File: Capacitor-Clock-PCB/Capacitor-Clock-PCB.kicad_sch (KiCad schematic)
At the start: 14 parts, among them J1 Jack-DC, J2 Conn_01x04, J3 Conn_01x02, J4 Conn_01x05, J5 Conn_01x02, J6 Conn_01x05, U2 DS3231M

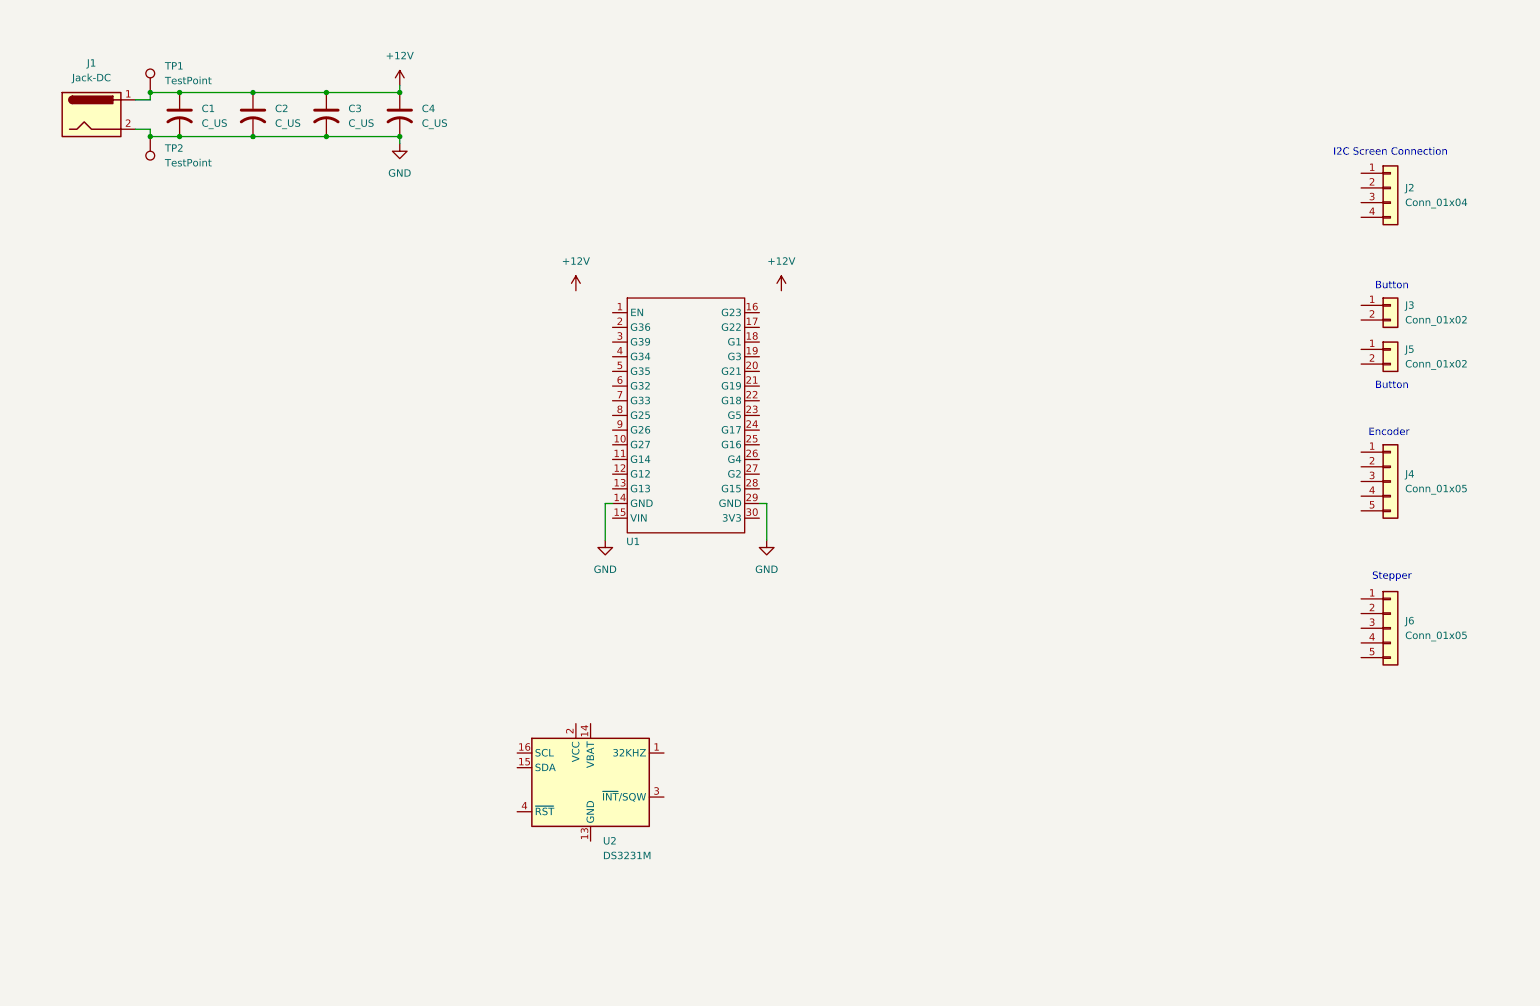
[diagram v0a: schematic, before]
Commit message: Preliminary Schematic Finished
Finished the schematic for the clock and is ready for review. going to continue to pcb layout in meantime
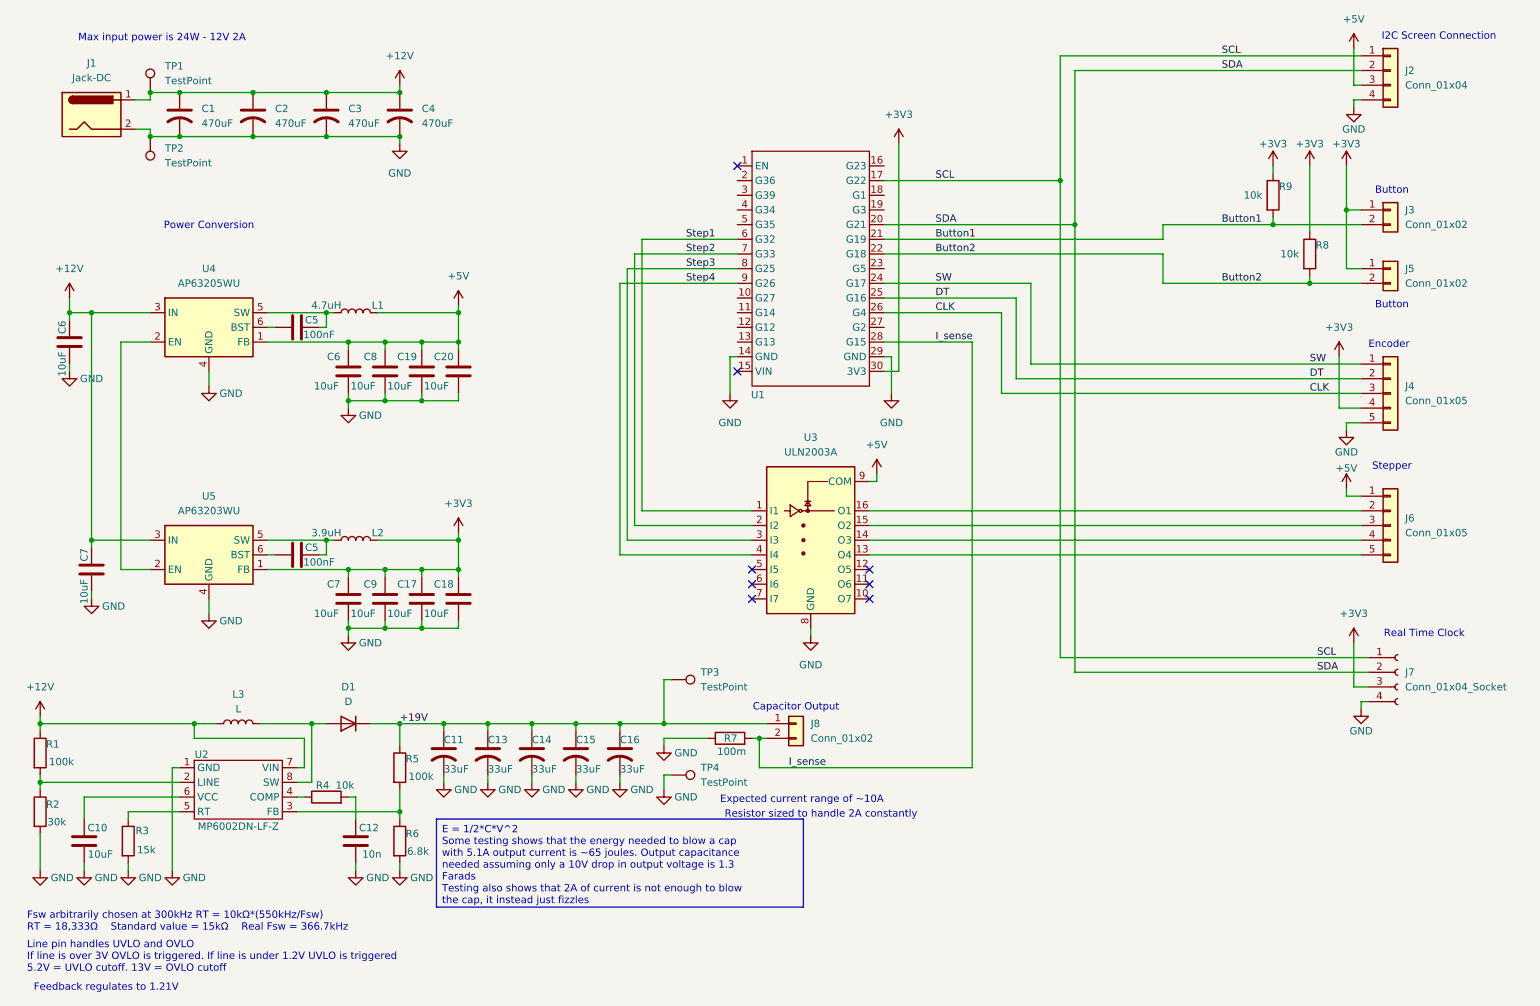
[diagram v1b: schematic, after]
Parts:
- removed U2: DS3231M, Package_SO:SOIC-16W_7.5x10.3mm_P1.27mm, symbol Timer_RTC:DS3231M
- added C10, C17, C18, C19, C20, C6 (x2), C7 (x2), C8, C9: 10uF, Capacitor_THT:C_Disc_D5.1mm_W3.2mm_P5.00mm, symbol Device:C
- added C11, C13, C14, C15, C16: 33uF, Capacitor_THT:CP_Radial_Tantal_D5.0mm_P2.50mm, symbol Device:C_US
- added C12: 10n, Capacitor_THT:C_Disc_D5.1mm_W3.2mm_P5.00mm, symbol Device:C
- added C5 (x2): 100nF, Capacitor_THT:C_Disc_D5.1mm_W3.2mm_P5.00mm, symbol Device:C
- added D1: D, symbol Device:D
- added J7: Conn_01x04_Socket, Connector_PinSocket_2.54mm:PinSocket_1x04_P2.54mm_Vertical, symbol Connector:Conn_01x04_Socket
- added J8: Conn_01x02, symbol Connector_Generic:Conn_01x02
- added L1: 4.7uH, SnapEDA Library:IND_SRR4818A-150M, symbol Device:L
- added L2: 3.9uH, SnapEDA Library:IND_SRR4818A-150M, symbol Device:L
- added L3: L, symbol Device:L
- added R1, R5: 100k, Resistor_THT:R_Axial_DIN0207_L6.3mm_D2.5mm_P7.62mm_Horizontal, symbol Device:R
- added R2: 30k, Resistor_THT:R_Axial_DIN0207_L6.3mm_D2.5mm_P7.62mm_Horizontal, symbol Device:R
- added R3: 15k, Resistor_THT:R_Axial_DIN0207_L6.3mm_D2.5mm_P7.62mm_Horizontal, symbol Device:R
- added R4, R8, R9: 10k, Resistor_THT:R_Axial_DIN0207_L6.3mm_D2.5mm_P7.62mm_Horizontal, symbol Device:R
- added R6: 6.8k, Resistor_THT:R_Axial_DIN0207_L6.3mm_D2.5mm_P7.62mm_Horizontal, symbol Device:R
- added R7: 100m, Resistor_SMD:R_Shunt_Vishay_WSK2512_6332Metric_T1.19mm, symbol Device:R
- added TP3, TP4: TestPoint, symbol Connector:TestPoint
- added U2: MP6002DN-LF-Z, Package_SO:SOIC-8-1EP_3.9x4.9mm_P1.27mm_EP2.41x3.3mm, symbol Dustins_Symbols:MP6002DN-LF-Z
- added U3: ULN2003A, Package_DIP:DIP-16_W7.62mm, symbol Transistor_Array:ULN2003A
- added U4: AP63205WU, Package_TO_SOT_SMD:TSOT-23-6, symbol Regulator_Switching:AP63205WU
- added U5: AP63203WU, Package_TO_SOT_SMD:TSOT-23-6, symbol Regulator_Switching:AP63203WU
- C1, C2, C3, C4: value C_US -> 470uF; footprint (none) -> Capacitor_THT:CP_Radial_Tantal_D8.0mm_P2.50mm
- J1: footprint (none) -> Connector_BarrelJack:BarrelJack_CUI_PJ-063AH_Horizontal
- J2: footprint (none) -> Connector_JST:JST_XH_B4B-XH-AM_1x04_P2.50mm_Vertical
- J3, J5: footprint (none) -> Connector_JST:JST_XH_B2B-XH-AM_1x02_P2.50mm_Vertical
- J4, J6: footprint (none) -> Connector_JST:JST_XH_B5B-XH-A_1x05_P2.50mm_Vertical
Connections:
- net +12V: now also C6.2, C7.2, L3.1, R1.1, U2.7 (VIN), U4.3 (IN), U5.3 (IN)
- net GND: now also J2.4 (Pin_4), J4.5 (Pin_5), C10.1, C11.2, C12.1, C13.2, C14.2, C15.2, C16.2, C17.1, C18.1, C19.1, C20.1, C6.1, C6.1, C7.1, C7.1, C8.1, C9.1, J7.4 (Pin_4), R2.2, R3.2, R6.2, R7.1, TP4.1, U2.1 (GND), U3.8 (GND), U4.4 (GND), U5.4 (GND)
- net +5V: now reaches J6.1 (Pin_1)
- net +5V: now also J2.3 (Pin_3), C19.2, C20.2, C6.2, C8.2, L1.2, U3.9 (COM), U4.1 (FB)
- net at J6.2 (Pin_2): now also U3.16 (O1)
- net at J6.3 (Pin_3): now also U3.15 (O2)
- net at J6.4 (Pin_4): now also U3.14 (O3)
- net at J6.5 (Pin_5): now also U3.13 (O4)
- net SW: now reaches J4.1 (Pin_1)
- net SW: now also U1.24 (G17)
- net DT: now reaches J4.2 (Pin_2)
- net DT: now also U1.25 (G16)
- net CLK: now reaches J4.3 (Pin_3)
- net CLK: now also U1.26 (G4)
- net +3V3: now reaches J4.4 (Pin_4)
- net +3V3: now also J3.1 (Pin_1), J5.1 (Pin_1), U1.30 (3V3), C17.2, C18.2, C7.2, C9.2, J7.3 (Pin_3), L2.2, R8.1, R9.1, U5.1 (FB)
- net SCL: now reaches J2.1 (Pin_1)
- net SCL: now also U1.17 (G22), J7.1 (Pin_1)
- net SDA: now reaches J2.2 (Pin_2)
- net SDA: now also U1.20 (G21), J7.2 (Pin_2)
- net Button1: now reaches U1.21 (G19)
- net Button1: now also J3.2 (Pin_2), R9.2
- net Button2: now reaches U1.22 (G18)
- net Button2: now also J5.2 (Pin_2), R8.2
- net I_sense: now reaches U1.28 (G15)
- net I_sense: now also J8.2 (Pin_2), R7.2
- net Step1: now reaches U1.6 (G32)
- net Step1: now also U3.1 (I1)
- net Step2: now reaches U1.7 (G33)
- net Step2: now also U3.2 (I2)
- net Step3: now reaches U1.8 (G25)
- net Step3: now also U3.3 (I3)
- net Step4: now reaches U1.9 (G26)
- net Step4: now also U3.4 (I4)
- new net: C10.2, U2.6 (VCC)
- new net: R5.2, R6.1, U2.3 (FB)
- new net: R4.1, U2.4 (COMP)
- new net: C12.2, R4.2
- new net: U4.2 (EN), U5.2 (EN)
- new net: C5.2, L1.1, U4.5 (SW)
- new net: C5.1, U4.6 (BST)
- new net: C5.1, U5.6 (BST)
- new net: C5.2, L2.1, U5.5 (SW)
- new net: D1.2 (A), L3.2, U2.8 (SW)
- new net: R1.2, R2.1, U2.2 (LINE)
- new net: R3.1, U2.5 (RT)
- new net +19V: C11.1, C13.1, C14.1, C15.1, C16.1, D1.1 (K), J8.1 (Pin_1), R5.1, TP3.1
- no-connect marks 0 -> 8
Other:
- note added: "Capacitor Output"
- note added: "Expected current range of ~10A"
- note added: "Feedback regulates to 1.21V"
- note added: "Fsw arbitrarily chosen at 300kHz RT = 10kΩ*(550kHz/Fsw) RT = 18,333Ω Standard value = 15kΩ Real Fsw = 366.7kHz"
- note added: "Line pin handles UVLO and OVLO If line is over 3V OVLO is triggered. If line is under 1.2V UVLO is triggered 5.2V = UVLO cutoff. 13V = OVLO cutoff"
- note added: "Max input power is 24W - 12V 2A"
- note added: "Power Conversion"
- note added: "Real Time Clock"
- note added: "Resistor sized to handle 2A constantly"
- moved on the sheet: J2, J3, J4, J5, J6, U1

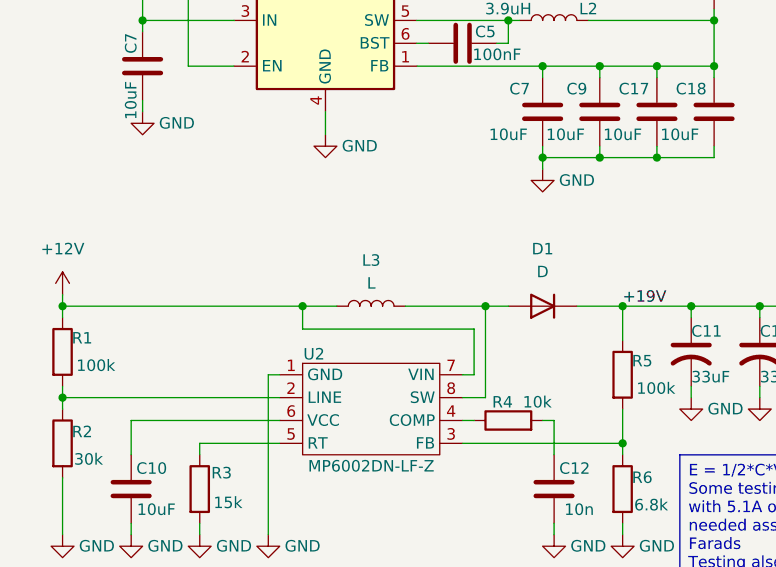
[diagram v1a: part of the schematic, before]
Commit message: picked induictor and diode
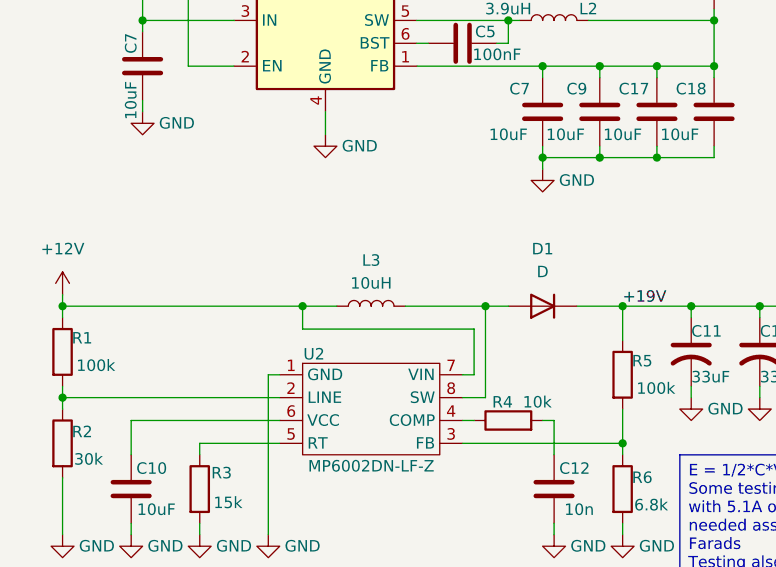
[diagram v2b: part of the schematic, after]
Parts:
- D1: footprint (none) -> Diode_THT:D_A-405_P7.62mm_Horizontal
- L3: value L -> 10uH; footprint (none) -> Inductor_THT:L_Radial_D8.7mm_P5.00mm_Fastron_07HCP
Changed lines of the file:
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@@
 			)
 		)
-		(property "Footprint" ""
+		(property "Footprint" "Diode_THT:D_A-405_P7.62mm_Horizontal"
 			(at 74.93 137.16 0)
 			(effects
@@
 			)
 		)
-		(property "Value" "L"
+		(property "Value" "10uH"
 			(at 55.88 134.62 90)
 			(effects
@@
 			)
 		)
-		(property "Footprint" ""
+		(property "Footprint" "Inductor_THT:L_Radial_D8.7mm_P5.00mm_Fastron_07HCP"
 			(at 55.88 137.16 0)
 			(effects
@@
 			)
 		)
-		(property "Description" "Inductor"
+		(property "Description" "RLB0914-100KL"
 			(at 55.88 137.16 0)
 			(effects

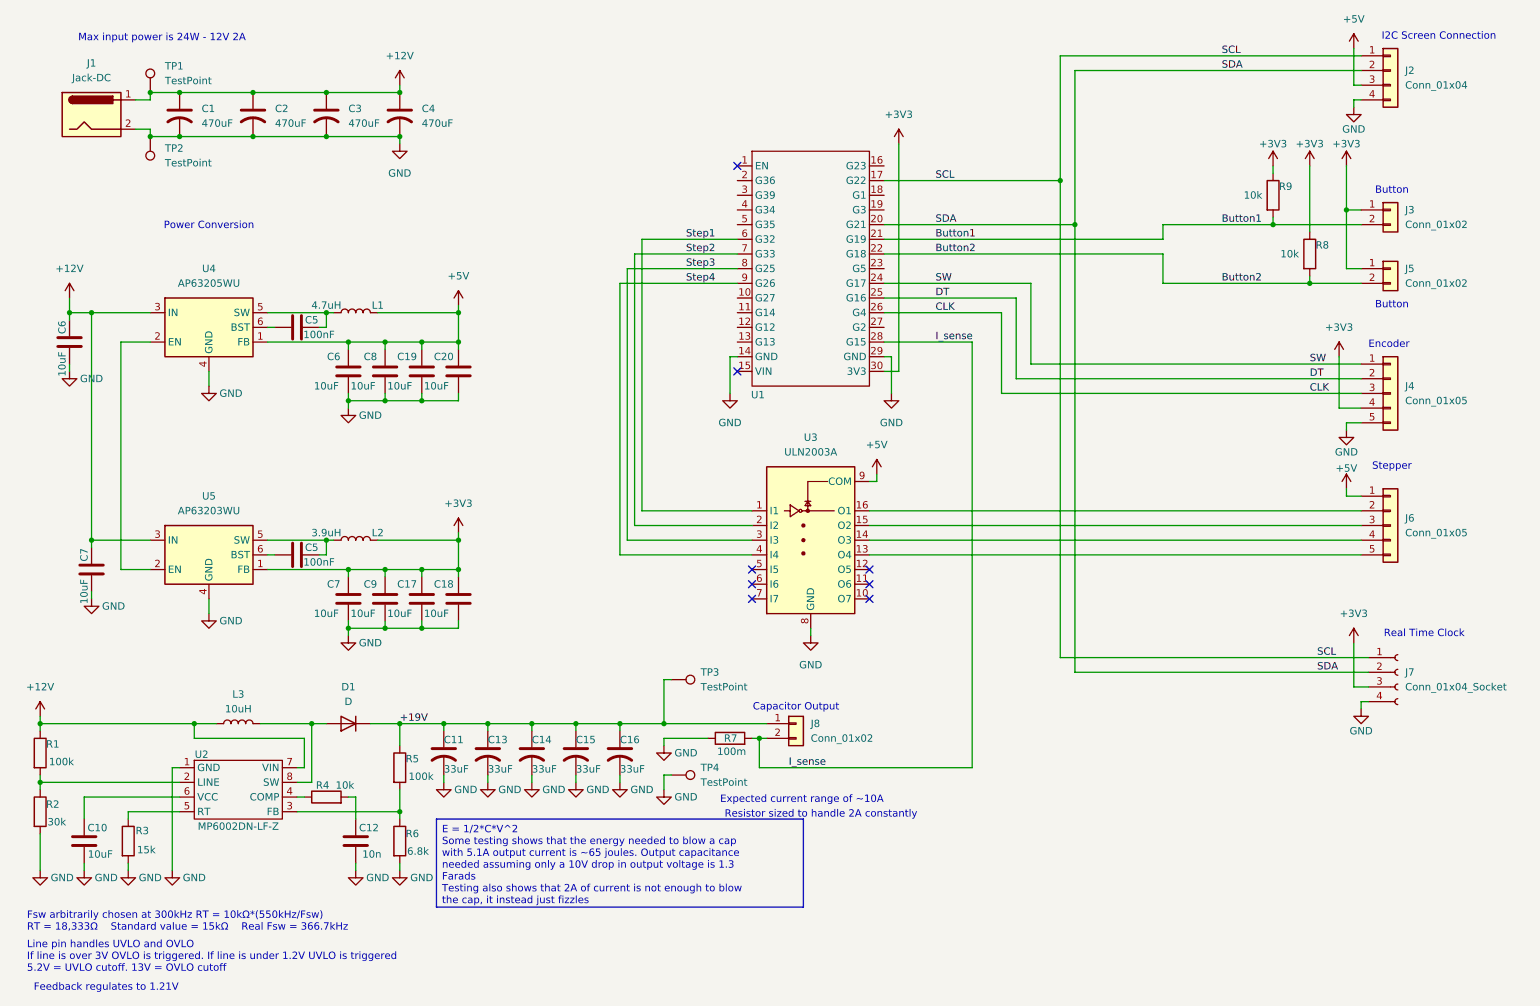
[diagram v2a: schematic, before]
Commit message: board component placement
finished preliminary component placement. ready for routing
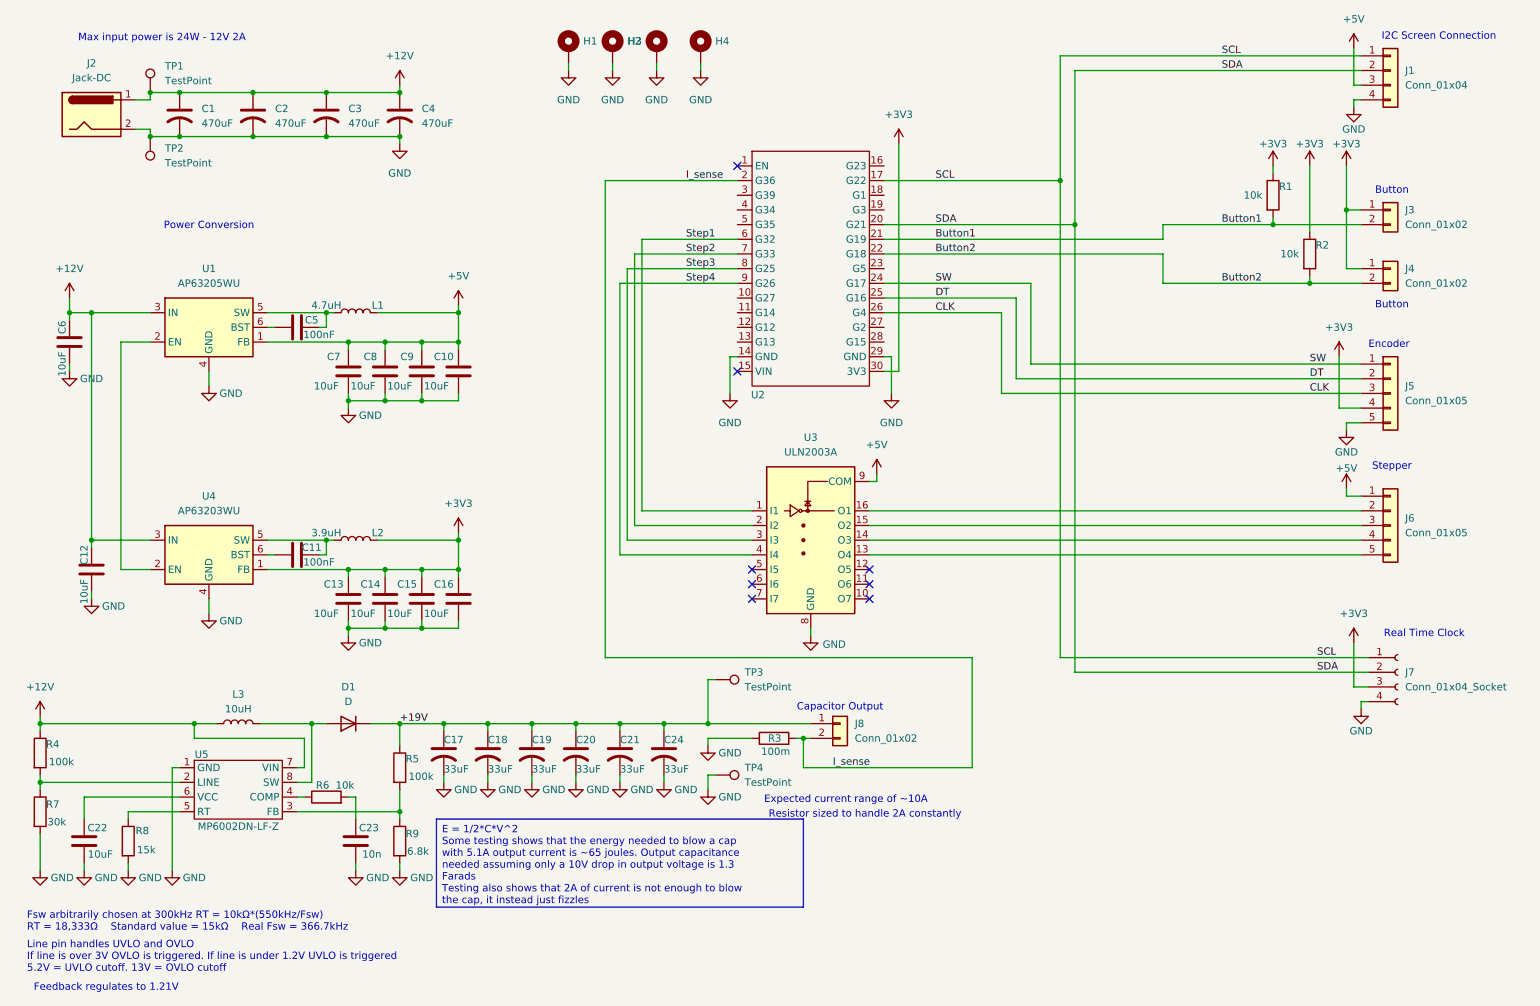
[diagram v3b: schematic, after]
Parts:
- added C24: 33uF, Capacitor_THT:CP_Radial_Tantal_D5.0mm_P2.50mm, symbol Device:C_US
- added H1, H2, H3, H4: MountingHole_Pad, MountingHole:MountingHole_3.2mm_M3_DIN965_Pad, symbol Mechanical:MountingHole_Pad
- J8: footprint (none) -> Connector_PinSocket_2.54mm:PinSocket_1x02_P2.54mm_Vertical
- L1, L2: footprint SnapEDA Library:IND_SRR4818A-150M -> SRR4818A-3R3Y:IND_SRR4818A-3R3Y
- R3: renamed from R7; footprint Resistor_SMD:R_Shunt_Vishay_WSK2512_6332Metric_T1.19mm -> Resistor_SMD:R_2512_6332Metric
- renumbered C20 to C10, C5 to C11, C7 to C12, C7 to C13, C9 to C14, C17 to C15, C18 to C16, C11 to C17, C13 to C18, C14 to C19, C15 to C20, C16 to C21, C10 to C22, C12 to C23, C6 to C7, C19 to C9, J2 to J1, J1 to J2, J5 to J4, J4 to J5, R9 to R1, R8 to R2, R1 to R4, R4 to R6, R2 to R7, R3 to R8, R6 to R9, U4 to U1, U1 to U2, U5 to U4, U2 to U5
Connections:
- net +19V: now also C24.1
- net GND: now also C24.2, H1.1, H2.1, H3.1, H4.1
- net I_sense: now also U2.2 (G36); no longer U2.28 (G15)
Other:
- moved on the sheet: J8, R3, TP3, TP4
